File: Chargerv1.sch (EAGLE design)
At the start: 12 parts, among them J1 POWER_JACKPTH_LOCK, U1 MCP73831, X1 USB-MICROB

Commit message: Routed Board
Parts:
- added JP2: M023.5MM, SparkFun-Connectors:M023.5MM
- added STANDOFF1, STANDOFF2, STANDOFF3, STANDOFF4: STAND-OFF, SparkFun-Electromechanical:STAND-OFF
- FRAME1: DESIGNER (none) -> Michelle
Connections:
- net 5V: now also JP2.1
- net GND: now also JP2.2
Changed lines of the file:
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@@
 <part name="GND3" library="SparkFun-Aesthetics" deviceset="GND" device=""/>
 <part name="GND4" library="SparkFun-Aesthetics" deviceset="GND" device=""/>
-<part name="FRAME1" library="SparkFun-Aesthetics" deviceset="FRAME-LETTER" device=""/>
+<part name="FRAME1" library="SparkFun-Aesthetics" deviceset="FRAME-LETTER" device="">
+<attribute name="DESIGNER" value="Michelle"/>
+</part>
 <part name="JP1" library="SparkFun-Connectors" deviceset="M02" device="-JST-2MM-SMT"/>
 <part name="JP3" library="SparkFun-Connectors" deviceset="M02" device="3.5MM"/>
@@
 <part name="GND6" library="SparkFun-Aesthetics" deviceset="GND" device=""/>
 <part name="GND7" library="SparkFun-Aesthetics" deviceset="GND" device=""/>
-<part name="SUPPLY1" library="SparkFun-Aesthetics" deviceset="5V" device=""/>
+<part name="5V" library="SparkFun-Aesthetics" deviceset="5V" device=""/>
 <part name="SUPPLY2" library="SparkFun-Aesthetics" deviceset="5V" device=""/>
 <part name="B1" library="Battery Holder 18650" deviceset="BATTERY" device="18650"/>
 <part name="SUPPLY3" library="SparkFun-Aesthetics" deviceset="V_BATT" device=""/>
 <part name="SUPPLY4" library="SparkFun-Aesthetics" deviceset="V_BATT" device=""/>
+<part name="JP2" library="SparkFun-Connectors" deviceset="M02" device="3.5MM"/>
+<part name="SUPPLY5" library="SparkFun-Aesthetics" deviceset="5V" device=""/>
+<part name="GND8" library="SparkFun-Aesthetics" deviceset="GND" device=""/>
+<part name="STANDOFF1" library="SparkFun-Electromechanical" deviceset="STAND-OFF" device=""/>
+<part name="STANDOFF2" library="SparkFun-Electromechanical" deviceset="STAND-OFF" device=""/>
+<part name="STANDOFF3" library="SparkFun-Electromechanical" deviceset="STAND-OFF" device=""/>
+<part name="STANDOFF4" library="SparkFun-Electromechanical" deviceset="STAND-OFF" device=""/>
 </parts>
 <sheets>
@@
 <instance part="GND3" gate="1" x="88.9" y="73.66"/>
 <instance part="GND4" gate="1" x="33.02" y="81.28"/>
-<instance part="FRAME1" gate="G$1" x="0" y="0"/>
+<instance part="FRAME1" gate="G$1" x="0" y="0">
+<attribute name="DESIGNER" x="0" y="0" size="1.778" layer="96" display="off"/>
+</instance>
 <instance part="FRAME1" gate="V" x="116.84" y="2.54"/>
 <instance part="JP1" gate="G$1" x="43.18" y="43.18" rot="R90"/>
@@
 <instance part="GND6" gate="1" x="33.02" y="101.6"/>
 <instance part="GND7" gate="1" x="12.7" y="30.48"/>
-<instance part="SUPPLY1" gate="G$1" x="33.02" y="127"/>
+<instance part="5V" gate="G$1" x="33.02" y="127"/>
 <instance part="SUPPLY2" gate="G$1" x="43.18" y="99.06"/>
 <instance part="B1" gate="B1" x="12.7" y="43.18" rot="R270"/>
 <instance part="SUPPLY3" gate="G$1" x="12.7" y="55.88"/>
 <instance part="SUPPLY4" gate="G$1" x="86.36" y="96.52"/>
+<instance part="JP2" gate="G$1" x="53.34" y="124.46" rot="MR180"/>
+<instance part="SUPPLY5" gate="G$1" x="60.96" y="132.08"/>
+<instance part="GND8" gate="1" x="60.96" y="111.76"/>
+<instance part="STANDOFF1" gate="G$1" x="180.34" y="33.02"/>
+<instance part="STANDOFF2" gate="G$1" x="185.42" y="33.02"/>
+<instance part="STANDOFF3" gate="G$1" x="190.5" y="33.02"/>
+<instance part="STANDOFF4" gate="G$1" x="195.58" y="33.02"/>
 </instances>
 <busses>
@@
 <wire x1="35.56" y1="50.8" x2="40.64" y2="50.8" width="0.1524" layer="91"/>
 </segment>
+<segment>
+<pinref part="JP2" gate="G$1" pin="2"/>
+<pinref part="GND8" gate="1" pin="GND"/>
+<wire x1="60.96" y1="121.92" x2="60.96" y2="114.3" width="0.1524" layer="91"/>
+</segment>
 </net>
 <net name="N$7" class="0">
@@
 <wire x1="25.4" y1="114.3" x2="33.02" y2="114.3" width="0.1524" layer="91"/>
 <wire x1="33.02" y1="114.3" x2="33.02" y2="127" width="0.1524" layer="91"/>
-<pinref part="SUPPLY1" gate="G$1" pin="5V"/>
+<pinref part="5V" gate="G$1" pin="5V"/>
 </segment>
 <segment>
@@
 <junction x="43.18" y="93.98"/>
 </segment>
+<segment>
+<pinref part="JP2" gate="G$1" pin="1"/>
+<wire x1="60.96" y1="132.08" x2="60.96" y2="124.46" width="0.1524" layer="91"/>
+<pinref part="SUPPLY5" gate="G$1" pin="5V"/>
+</segment>
 </net>

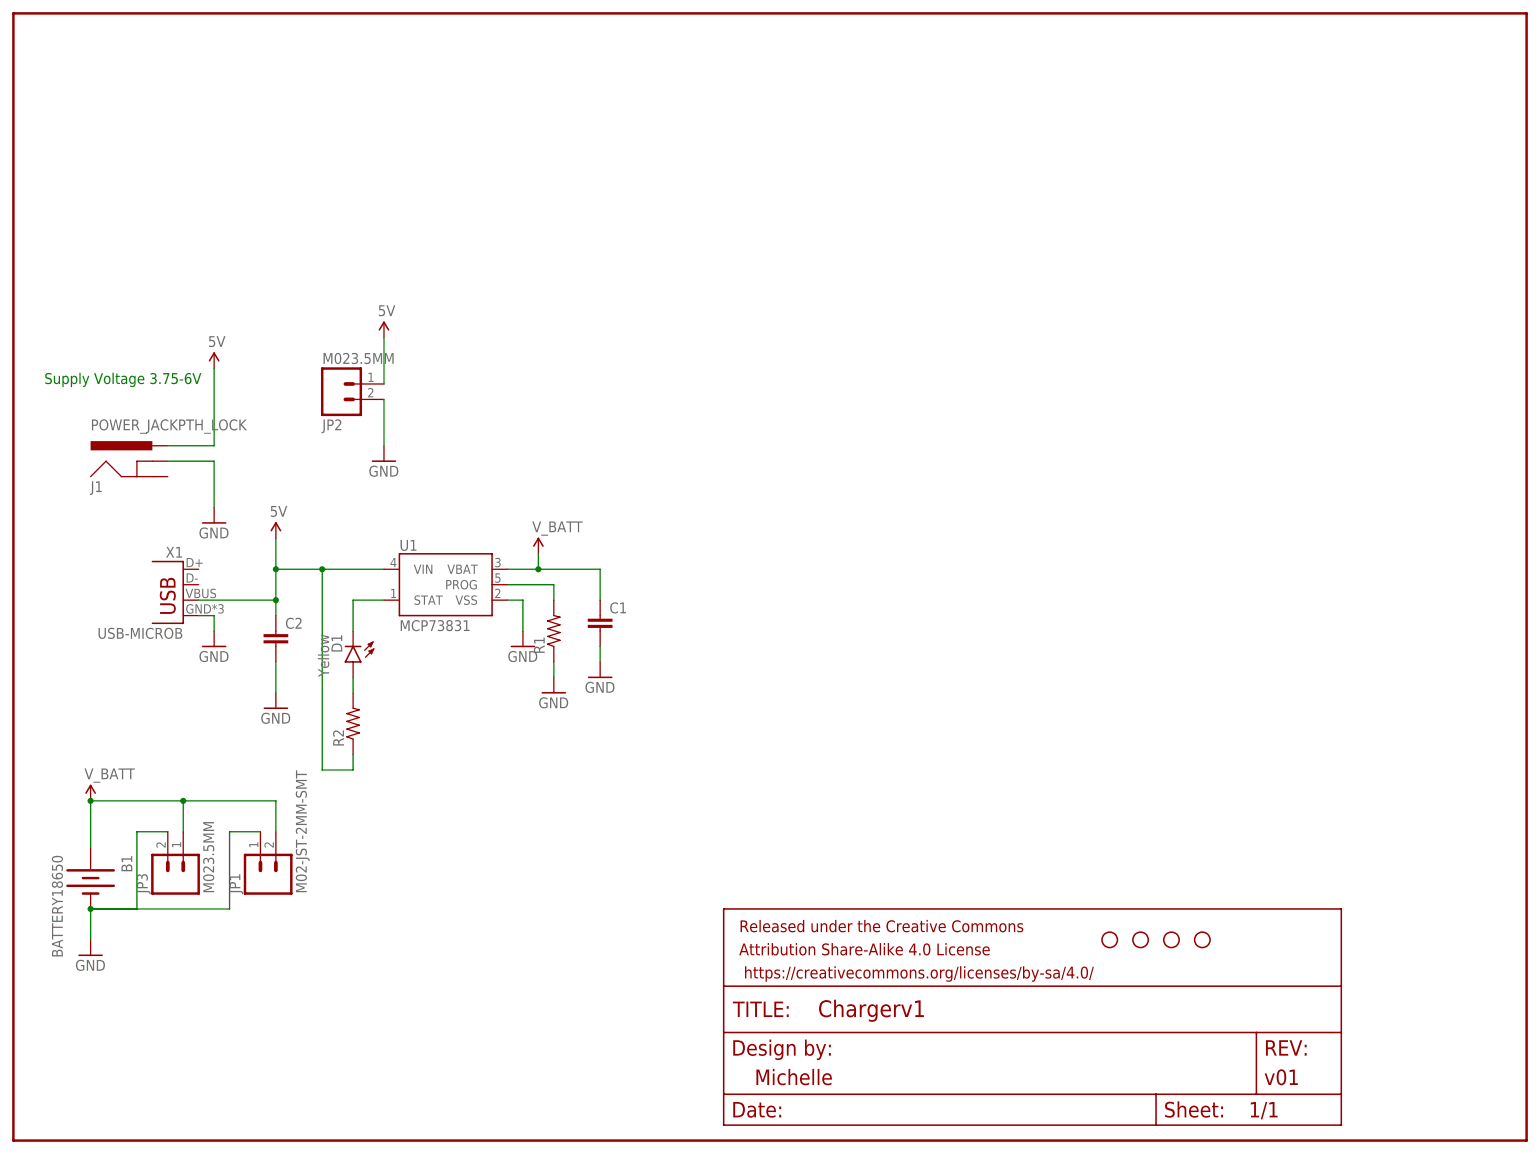
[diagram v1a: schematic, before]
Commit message: Ready for Itead order
Final version with gerbers as sent to Itead (ordered 1/30, received
2/11)
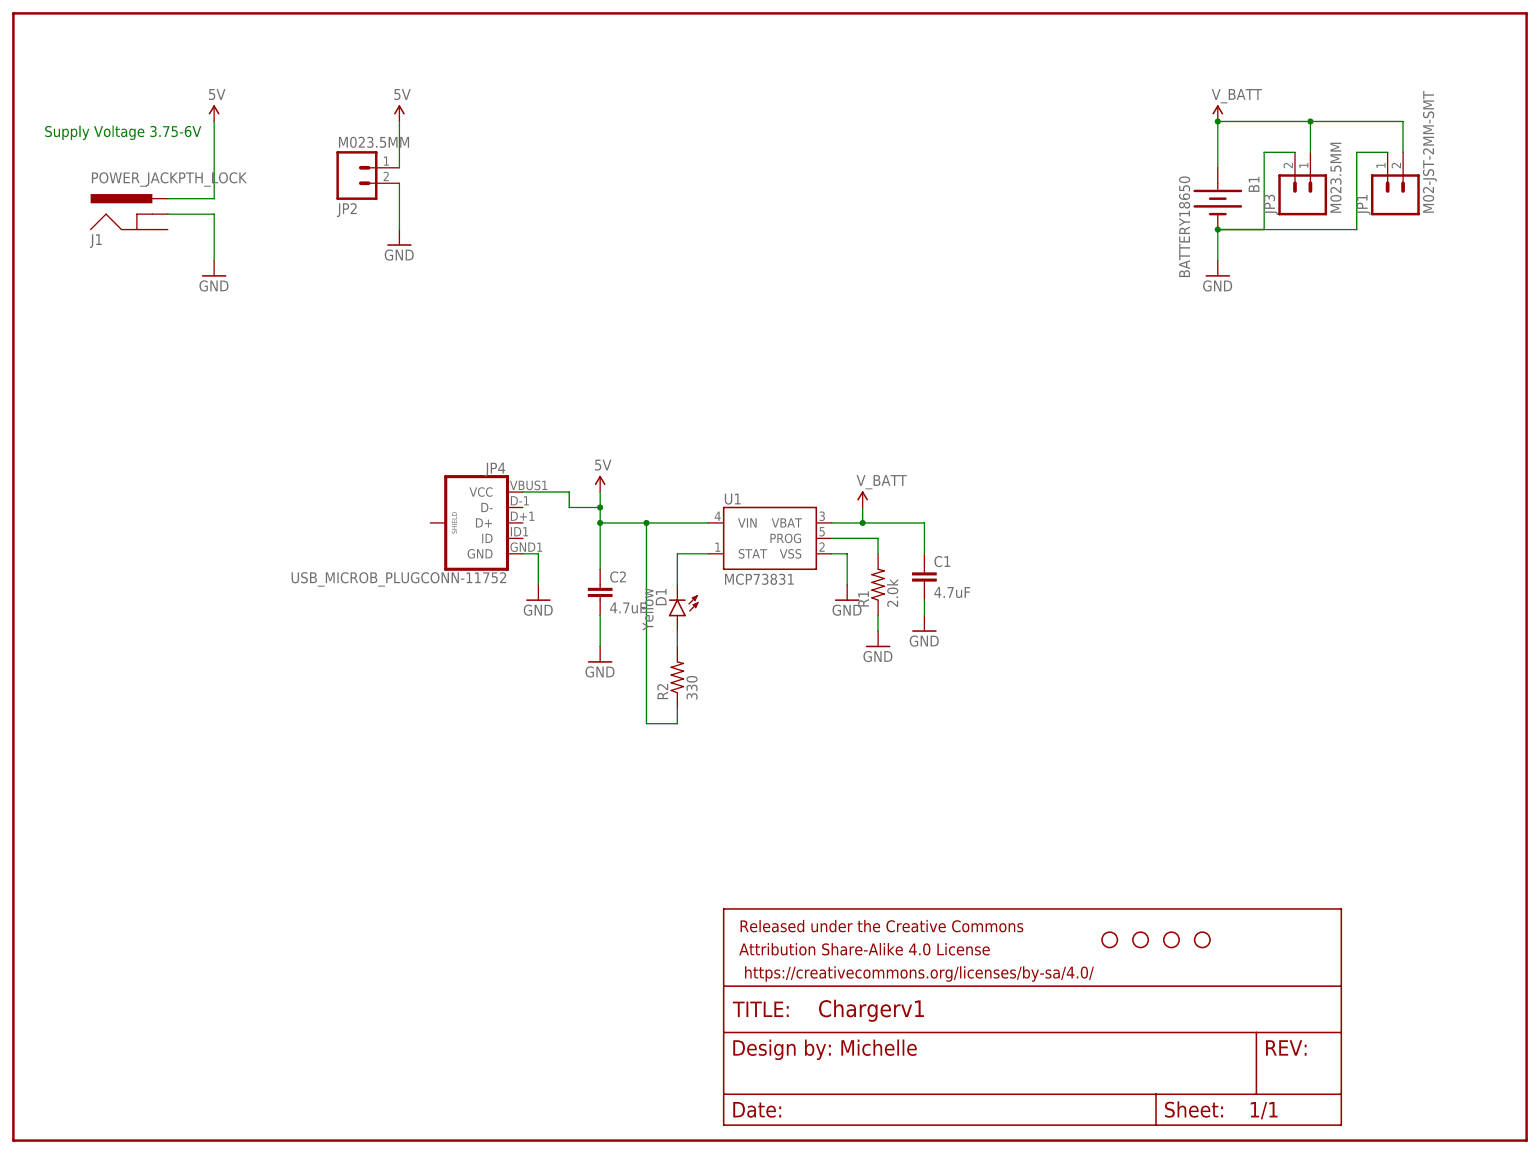
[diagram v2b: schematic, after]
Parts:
- removed X1: USB-MICROB, SparkFun-Connectors:USB-MICROB
- added JP4: USB_MICROB_PLUGCONN-11752, SparkFun-Connectors:USB_MICROB_PLUGCONN-11752
- C1, C2: value (none) -> 4.7uF; device SparkFun-Passives:CAP0603-CAP -> SparkFun-Capacitors:4.7UF-6.3V-10%(0603)0603
- R1: value (none) -> 2.0k; device SparkFun-Passives:RESISTOR0603-RES -> SparkFun-Resistors:2.0KOHM1/10W5%(0603)
- R2: value (none) -> 330; device SparkFun-Passives:RESISTOR0603-RES -> SparkFun-Resistors:330OHM1/10W1%(0603)
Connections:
- net 5V: now also JP4.VCC; no longer X1.VBUS
- net GND: now also JP4.GND; no longer X1.GND
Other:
- moved on the sheet: B1, C1, C2, D1, J1, JP1, JP2, JP3, R1, R2, U1
